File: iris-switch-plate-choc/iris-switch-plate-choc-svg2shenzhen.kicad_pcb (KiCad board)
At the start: 2 copper layers, 153.5 x 133.7 mm, 17 parts

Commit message: 図を用紙の中に移動
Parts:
- removed the ? at (-76.0, 26.0)
- removed the ? at (43.4, -8.30)
- removed the ? at (-10.2, 44.8)
- removed the ? at (45.8, 59.6)
- removed the ? at (69.3, 18.7)
- removed the ? at (43.0, -56.3)
- removed the ? at (22.4, -64.5)
- removed the ? at (-27.5, -65.1)
- removed the ? at (-76.2, -54.3)
- removed the ? at (55.6, 9.25)
- removed the G*** at (0.00, 0.00) (x7)
- added ?: , Wire_Pads:SolderWirePad_single_0-8mmDrill, F.Cu at (114.0, 121.0)
- added ?: , Wire_Pads:SolderWirePad_single_0-8mmDrill, F.Cu at (233.4, 86.7)
- added ?: , Wire_Pads:SolderWirePad_single_0-8mmDrill, F.Cu at (179.8, 139.8)
- added ?: , Wire_Pads:SolderWirePad_single_0-8mmDrill, F.Cu at (235.8, 154.6)
- added ?: , Wire_Pads:SolderWirePad_single_0-8mmDrill, F.Cu at (259.3, 113.7)
- added ?: , Wire_Pads:SolderWirePad_single_0-8mmDrill, F.Cu at (233.0, 38.7)
- added ?: , Wire_Pads:SolderWirePad_single_0-8mmDrill, F.Cu at (212.4, 30.5)
- added ?: , Wire_Pads:SolderWirePad_single_0-8mmDrill, F.Cu at (162.5, 29.9)
- added ?: , Wire_Pads:SolderWirePad_single_0-8mmDrill, F.Cu at (113.8, 40.7)
- added ?: , Wire_Pads:SolderWirePad_single_0-8mmDrill, F.Cu at (245.6, 104.3)
- added G*** (x4): LOGO, LOGO, F.Cu at (190.0, 95.0)
- added G*** (x3): LOGO, LOGO, F.Cu at (0.00, 0.00)

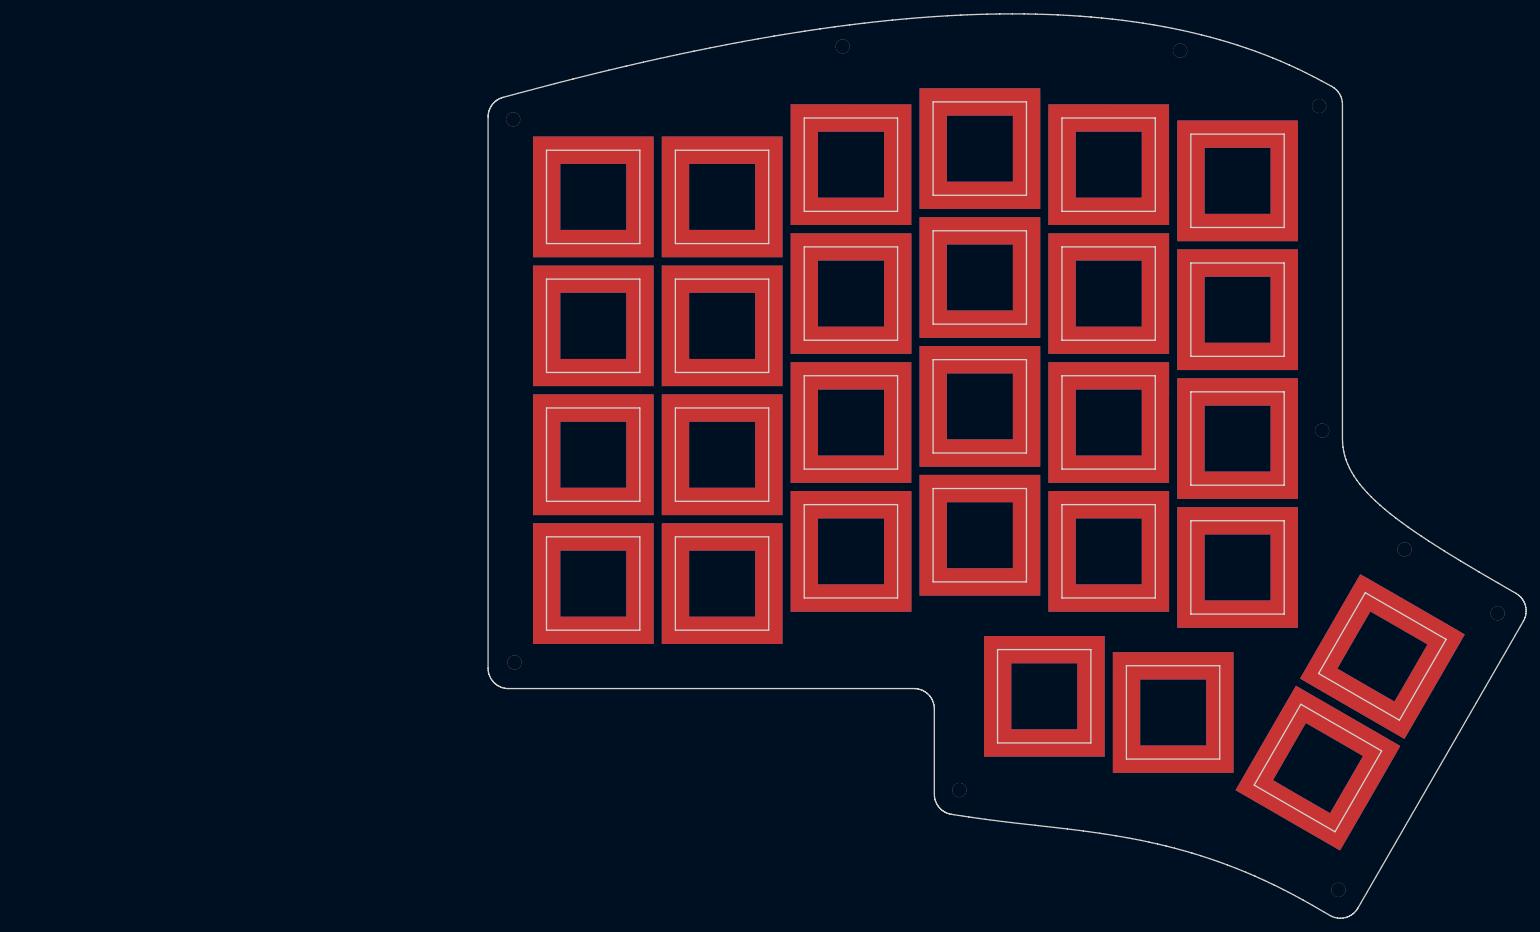
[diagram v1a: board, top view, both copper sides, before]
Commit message: 外板付けて、外形をざっくり採寸
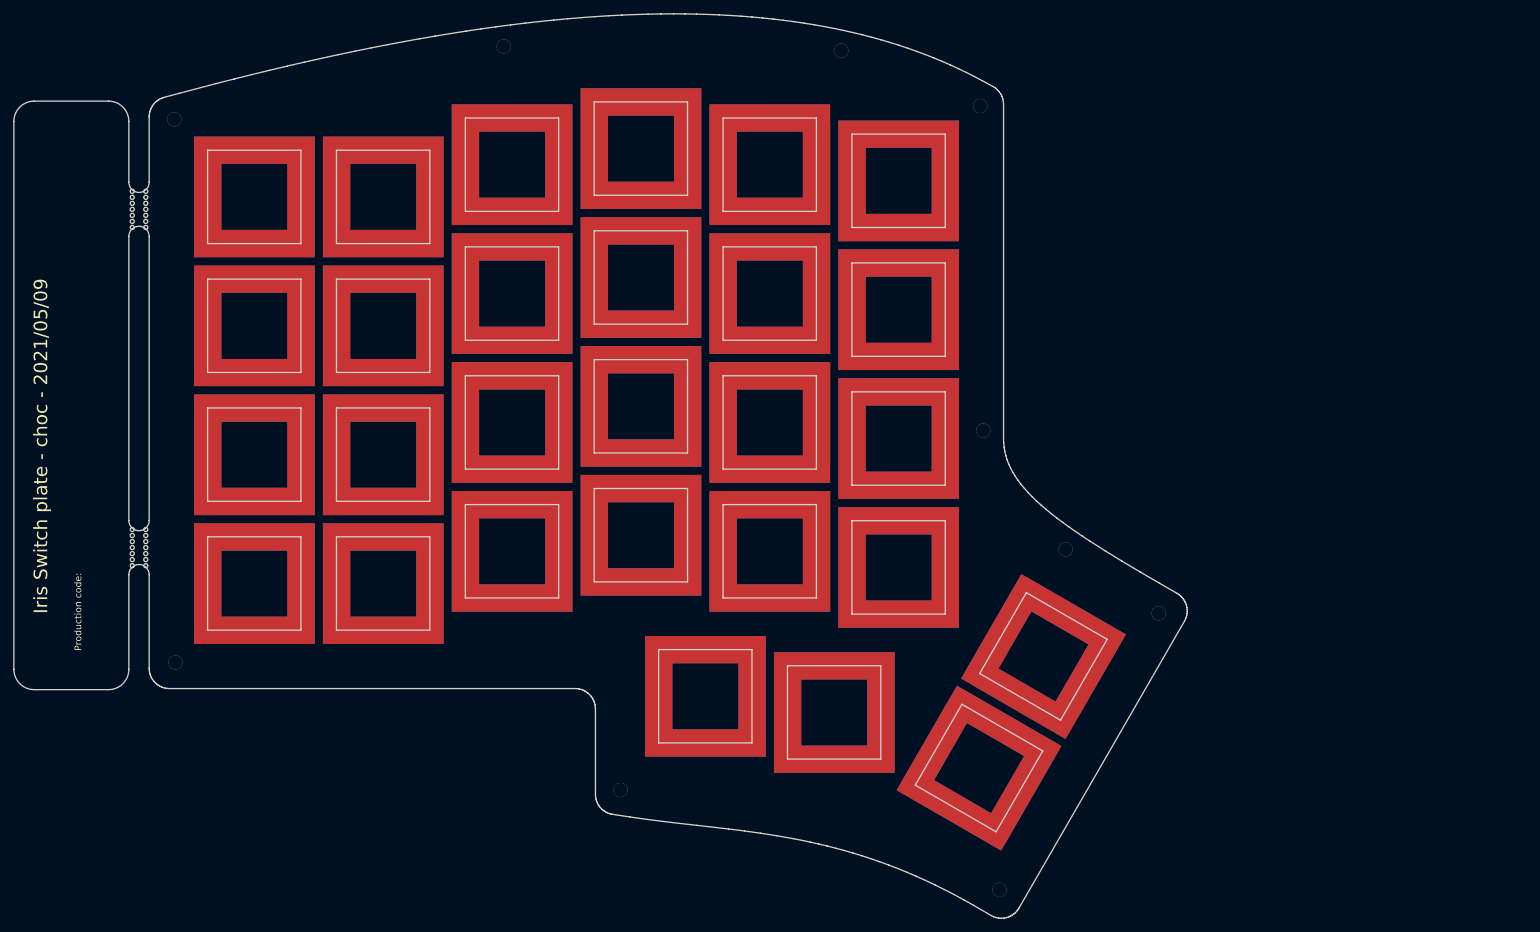
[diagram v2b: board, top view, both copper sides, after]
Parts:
- removed the ? at (114.0, 121.0)
- removed the ? at (233.4, 86.7)
- removed the ? at (179.8, 139.8)
- removed the ? at (235.8, 154.6)
- removed the ? at (259.3, 113.7)
- removed the ? at (233.0, 38.7)
- removed the ? at (212.4, 30.5)
- removed the ? at (162.5, 29.9)
- removed the ? at (113.8, 40.7)
- removed the ? at (245.6, 104.3)
- removed the G*** at (190.0, 95.0) (x4)
- removed the G*** at (0.00, 0.00) (x3)
- added ?: , Wire_Pads:SolderWirePad_single_0-8mmDrill, F.Cu at (63.9, 121.0)
- added ?: , Wire_Pads:SolderWirePad_single_0-8mmDrill, F.Cu at (183.3, 86.7)
- added ?: , Wire_Pads:SolderWirePad_single_0-8mmDrill, F.Cu at (129.7, 139.8)
- added ?: , Wire_Pads:SolderWirePad_single_0-8mmDrill, F.Cu at (185.7, 154.6)
- added ?: , Wire_Pads:SolderWirePad_single_0-8mmDrill, F.Cu at (209.2, 113.7)
- added ?: , Wire_Pads:SolderWirePad_single_0-8mmDrill, F.Cu at (182.9, 38.7)
- added ?: , Wire_Pads:SolderWirePad_single_0-8mmDrill, F.Cu at (162.3, 30.5)
- added ?: , Wire_Pads:SolderWirePad_single_0-8mmDrill, F.Cu at (112.4, 29.9)
- added ?: , Wire_Pads:SolderWirePad_single_0-8mmDrill, F.Cu at (63.7, 40.7)
- added ?: , Wire_Pads:SolderWirePad_single_0-8mmDrill, F.Cu at (195.5, 104.3)
- added G*** (x4): LOGO, LOGO, F.Cu at (139.9, 95.0)
- added G*** (x3): LOGO, LOGO, F.Cu at (0.00, 0.00)
- added REF**: Mouse_Bites_3.00_5.00, mouse-bites:Mouse_Bites_3.00_5.00, F.Cu at (58.5, 104.0)
- added REF**: Mouse_Bites_3.00_5.00, mouse-bites:Mouse_Bites_3.00_5.00, F.Cu at (58.5, 54.0)
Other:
- board size 153.5 x 133.7 mm -> 173.5 x 133.7 mm
- board text added: "Iris Switch plate - choc - 2021/05/09"
- board text added: "Production code:"

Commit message: FusionPCB の流儀でガーバーデータを出力
cf. https://www.fusionpcb.jp/blog/?p=1178
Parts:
- removed the G*** at (139.9, 95.0) (x4)
- removed the G*** at (0.00, 0.00) (x3)
- added G*** (x4): LOGO, LOGO, F.Cu at (139.9, 95.0)
- added G*** (x3): LOGO, LOGO, F.Cu at (0.00, 0.00)
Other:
- rule pad_to_mask_clearance: 0.2 -> 0
